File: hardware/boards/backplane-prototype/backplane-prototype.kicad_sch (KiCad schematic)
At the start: 7 parts

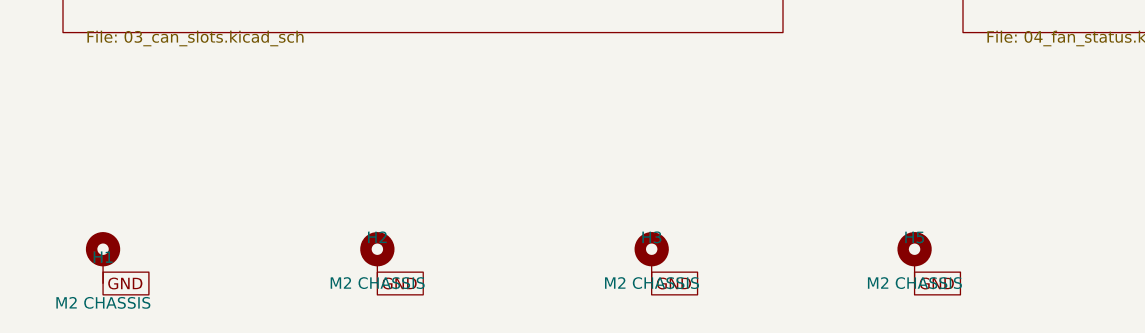
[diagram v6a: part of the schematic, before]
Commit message: checkpoint backplane PCB synchronization
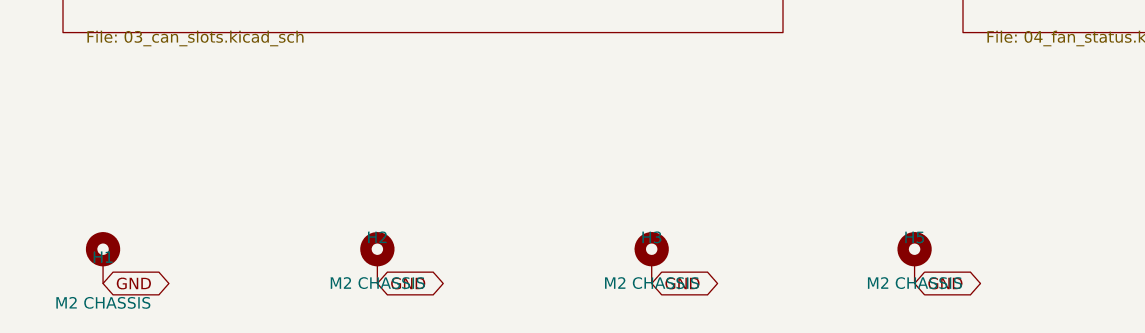
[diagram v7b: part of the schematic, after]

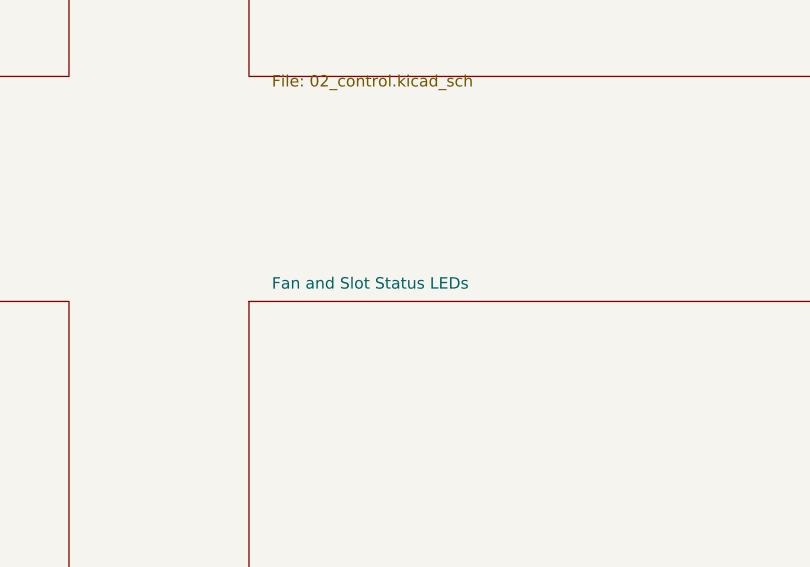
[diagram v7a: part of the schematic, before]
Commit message: hardware: add backplane thermal interfaces
Add a second independent 3-wire fan channel and externally powered DS18B20 header, remove the slot NeoPixels, document the shared fan-rail limits, keep test points out of assembly exports, and move the four chassis holes to their nearest DRC-legal edge positions.
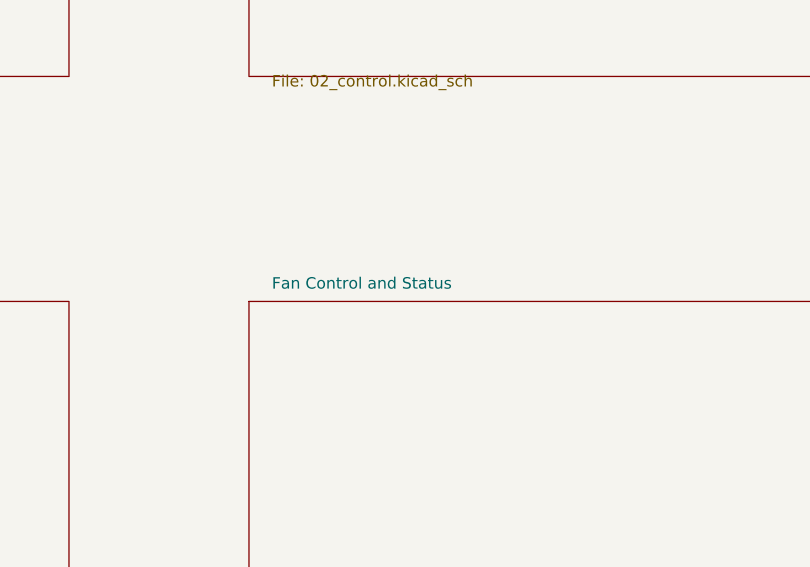
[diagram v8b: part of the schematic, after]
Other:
- sheet Fan and Slot Status LEDs renamed Fan Control and Status
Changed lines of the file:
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@@
 			(color 0 0 0 0)
 		)
-		(property "Sheetname" "Fan and Slot Status LEDs"
+		(property "Sheetname" "Fan Control and Status"
 			(at 142.54 108.73 0)
 			(show_name no)
